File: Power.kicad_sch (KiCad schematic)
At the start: 11 parts, among them J14 Conn_01x02, U4 TPS62130

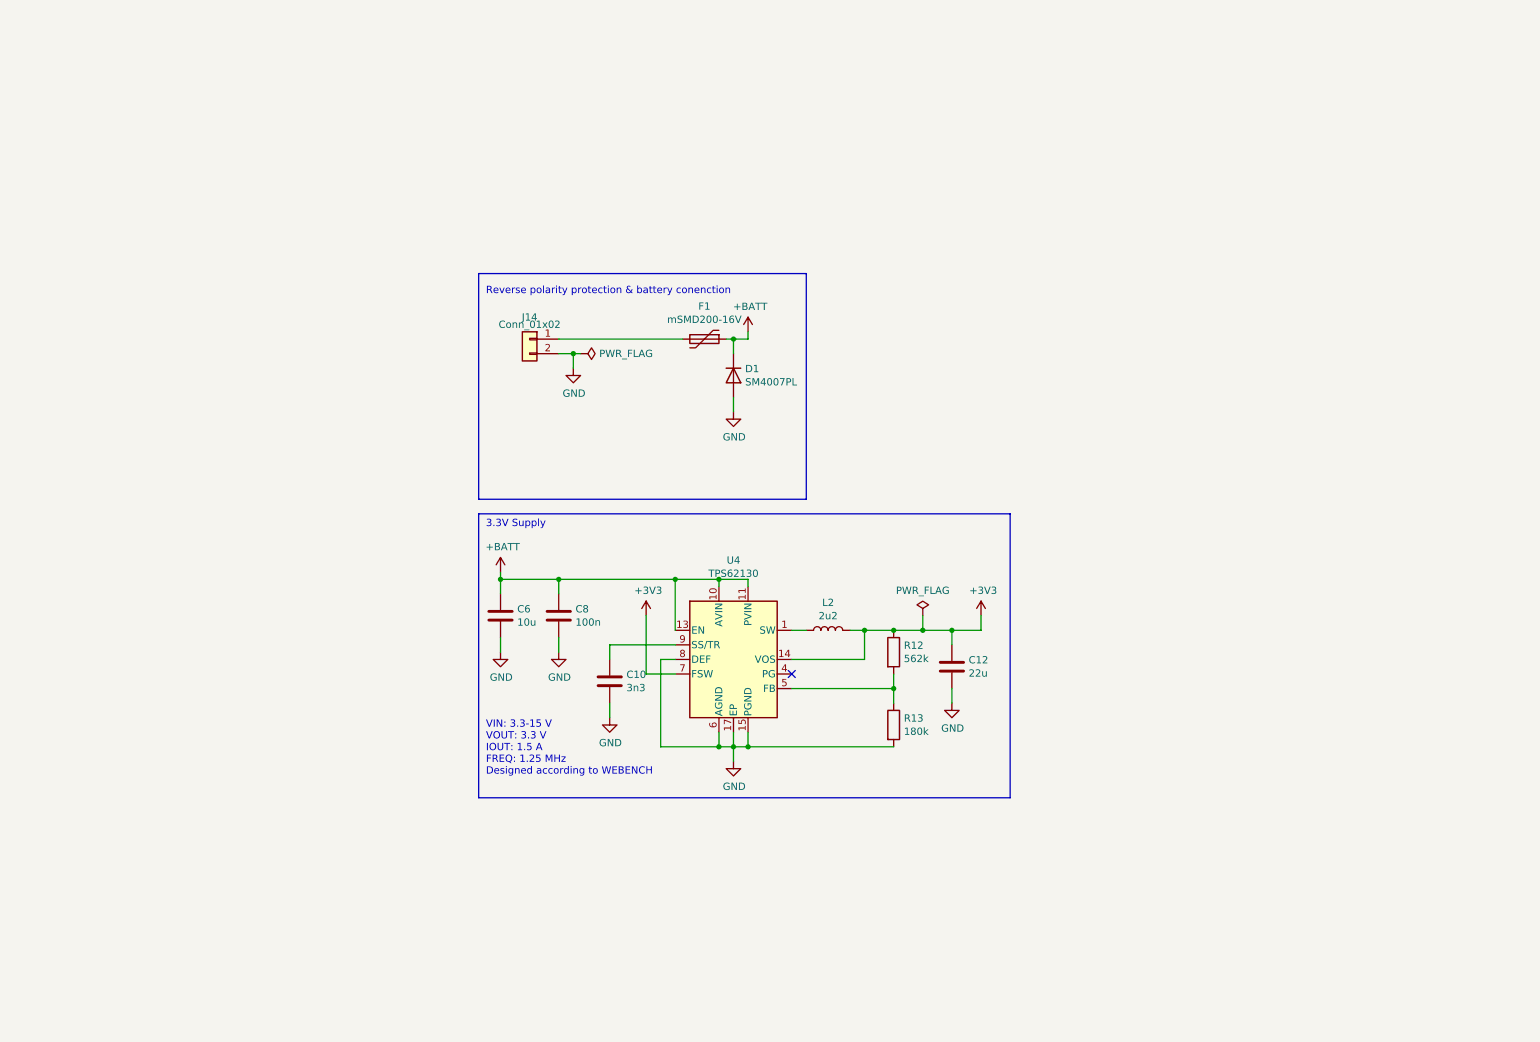
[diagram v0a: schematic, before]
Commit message: Move to KiCad v6, redesign circuit for chamber
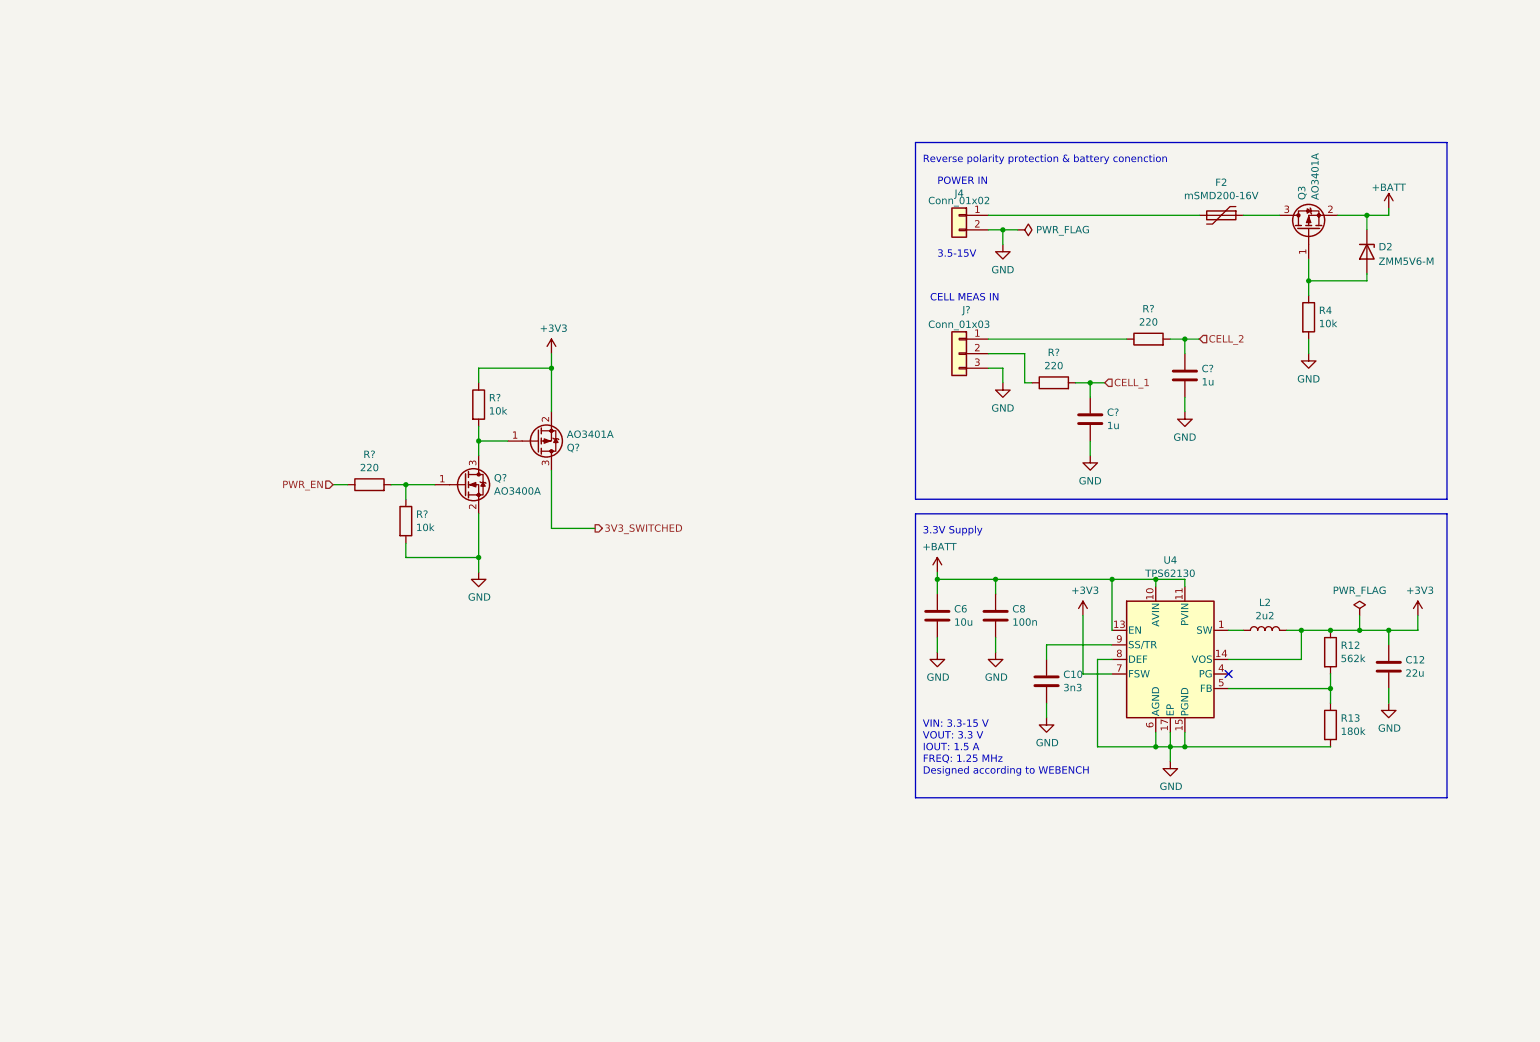
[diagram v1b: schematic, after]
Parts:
- removed D1: SM4007PL, Diode_SMD:D_SOD-123F, symbol Device:D
- removed F1: mSMD200-16V, Fuse:Fuse_1812_4532Metric, symbol Device:Polyfuse
- removed J14: Conn_01x02, Connector_JST:JST_XH_B2B-XH-AM_1x02_P2.50mm_Vertical, symbol Connector_Generic:Conn_01x02
- added C? (x2): 1u, Capacitor_SMD:C_0603_1608Metric, symbol Device:C
- added D2: ZMM5V6-M, Diode_SMD:D_MiniMELF, symbol Device:D_Zener
- added F2: mSMD200-16V, Fuse:Fuse_1812_4532Metric, symbol Device:Polyfuse
- added J4: Conn_01x02, Connector_JST:JST_XH_B2B-XH-AM_1x02_P2.50mm_Vertical, symbol Connector_Generic:Conn_01x02
- added J?: Conn_01x03, Connector_JST:JST_XH_B3B-XH-AM_1x03_P2.50mm_Vertical, symbol Connector_Generic:Conn_01x03
- added Q3, Q?: AO3401A, Package_TO_SOT_SMD:SOT-23, symbol Transistor_FET:AO3401A
- added Q?: AO3400A, Package_TO_SOT_SMD:SOT-23, symbol Transistor_FET:AO3400A
- added R4, R? (x2): 10k, Resistor_SMD:R_0603_1608Metric, symbol Device:R
- added R? (x3): 220, Resistor_SMD:R_0603_1608Metric, symbol Device:R
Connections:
- net +3V3: now also Q?.2 (S), R?.1
- net +BATT: now also D2.1 (K), Q3.2 (S)
- net GND: now also C?.2, C?.2, J4.2 (Pin_2), J?.3 (Pin_3), Q?.2 (S), R4.2, R?.2
- new net: D2.2 (A), Q3.1 (G), R4.1
- new net: F2.2, J4.1 (Pin_1)
- new net: F2.1, Q3.3 (D)
- new net: Q?.1 (G), R?.1, R?.2
- new net: Q?.1 (G), Q?.3 (D), R?.2
- new net: J?.1 (Pin_1), R?.1
- new net: J?.2 (Pin_2), R?.1
- new net 3V3_SWITCHED: Q?.3 (D)
- new net CELL_1: C?.1, R?.2
- new net CELL_2: C?.1, R?.2
- new net PWR_EN: R?.1
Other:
- note added: "3.5-15V"
- note added: "CELL MEAS IN"
- note added: "POWER IN"
- moved on the sheet: C10, C12, C6, C8, L2, R12, R13, U4

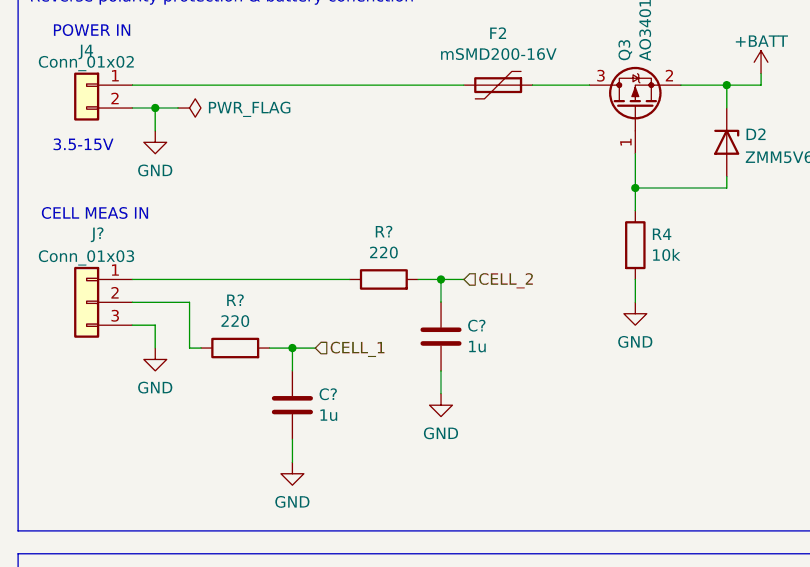
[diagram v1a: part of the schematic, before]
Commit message: Add test points, add JLC part numbers to JST XH connectors, clean up
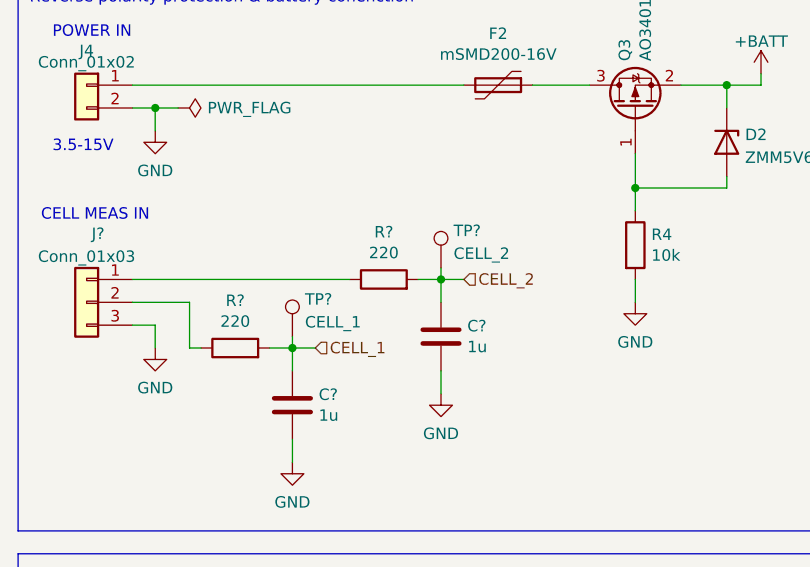
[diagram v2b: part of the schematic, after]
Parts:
- added TP?: CELL_1, symbol Connector:TestPoint
- added TP?: CELL_2, symbol Connector:TestPoint
- J4: LCSC (none) -> C20079
- J?: LCSC (none) -> C2316
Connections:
- net CELL_1: now also TP?.1
- net CELL_2: now also TP?.1
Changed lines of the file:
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@@
+    (stroke (width 0) (type default) (color 0 0 0 0))
+  )
+  (wire (pts (xy 220.98 71.12) (xy 220.98 72.39))
     (stroke (width 0) (type default) (color 0 0 0 0))
   )
@@
   )
   (wire (pts (xy 208.28 123.19) (xy 208.28 114.3))
+    (stroke (width 0) (type default) (color 0 0 0 0))
+  )
+  (wire (pts (xy 204.47 78.74) (xy 204.47 80.01))
     (stroke (width 0) (type default) (color 0 0 0 0))
   )
@@
       (effects (font (size 1.27 1.27)) hide)
     )
+    (property "LCSC" "C20079" (id 4) (at 181.61 50.8 0)
+      (effects (font (size 1.27 1.27)) hide)
+    )
     (pin "1")
     (pin "2")
@@
     (pin "2")
   )
+  (symbol (lib_id "Connector:TestPoint") (at 204.47 78.74 0) (unit 1)
+    (in_bom yes) (on_board yes) (fields_autoplaced)
+    (property "Reference" "TP?" (id 0) (at 205.867 74.6033 0)
+      (effects (font (size 1.27 1.27)) (justify left))
+    )
+    (property "Value" "CELL_1" (id 1) (at 205.867 77.1402 0)
+      (effects (font (size 1.27 1.27)) (justify left))
+    )
+    (property "Footprint" "" (id 2) (at 209.55 78.74 0)
+      (effects (font (size 1.27 1.27)) hide)
+    )
+    (property "Datasheet" "~" (id 3) (at 209.55 78.74 0)
+      (effects (font (size 1.27 1.27)) hide)
+    )
+    (pin "1")
+  )
   (symbol (lib_id "power:+3V3") (at 110.49 74.93 0) (unit 1)
     (in_bom yes) (on_board yes)
@@
       (effects (font (size 1.27 1.27)) hide)
     )
+    (property "LCSC" "C2316" (id 4) (at 181.61 74.93 0)
+      (effects (font (size 1.27 1.27)) hide)
+    )
     (pin "1")
     (pin "2")
@@
     (pin "3")
   )
+  (symbol (lib_id "Connector:TestPoint") (at 220.98 71.12 0) (unit 1)
+    (in_bom yes) (on_board yes) (fields_autoplaced)
+    (property "Reference" "TP?" (id 0) (at 222.377 66.9833 0)
+      (effects (font (size 1.27 1.27)) (justify left))
+    )
+    (property "Value" "CELL_2" (id 1) (at 222.377 69.5202 0)
+      (effects (font (size 1.27 1.27)) (justify left))
+    )
+    (property "Footprint" "" (id 2) (at 226.06 71.12 0)
+      (effects (font (size 1.27 1.27)) hide)
+    )
+    (property "Datasheet" "~" (id 3) (at 226.06 71.12 0)
+      (effects (font (size 1.27 1.27)) hide)
+    )
+    (pin "1")
+  )
   (symbol (lib_id "power:PWR_FLAG") (at 191.77 53.34 270) (unit 1)

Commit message: Add testpoint footprint assignments
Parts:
- TP16, TP17: renamed from TP?; footprint (none) -> TestPoint:TestPoint_Loop_D2.50mm_Drill1.0mm_LowProfile
- gave numbers to parts that had none: 10
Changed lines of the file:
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@@
   (symbol (lib_id "power:GND") (at 97.79 113.03 0) (unit 1)
     (in_bom yes) (on_board yes)
-    (property "Reference" "#PWR?" (id 0) (at 97.79 119.38 0)
+    (property "Reference" "#PWR0119" (id 0) (at 97.79 119.38 0)
       (effects (font (size 1.27 1.27)) hide)
     )
@@
   (symbol (lib_id "power:GND") (at 189.23 80.01 0) (unit 1)
     (in_bom yes) (on_board yes) (fields_autoplaced)
-    (property "Reference" "#PWR?" (id 0) (at 189.23 86.36 0)
+    (property "Reference" "#PWR0122" (id 0) (at 189.23 86.36 0)
       (effects (font (size 1.27 1.27)) hide)
     )
@@
   (symbol (lib_id "Device:R") (at 85.09 104.14 0) (unit 1)
     (in_bom yes) (on_board yes)
-    (property "Reference" "R?" (id 0) (at 86.868 102.9716 0)
+    (property "Reference" "R5" (id 0) (at 86.868 102.9716 0)
       (effects (font (size 1.27 1.27)) (justify left))
     )
@@
   (symbol (lib_id "Connector:TestPoint") (at 204.47 78.74 0) (unit 1)
     (in_bom yes) (on_board yes) (fields_autoplaced)
-    (property "Reference" "TP?" (id 0) (at 205.867 74.6033 0)
+    (property "Reference" "TP16" (id 0) (at 205.867 74.6033 0)
       (effects (font (size 1.27 1.27)) (justify left))
     )
@@
       (effects (font (size 1.27 1.27)) (justify left))
     )
-    (property "Footprint" "" (id 2) (at 209.55 78.74 0)
+    (property "Footprint" "TestPoint:TestPoint_Loop_D2.50mm_Drill1.0mm_LowProfile" (id 2) (at 209.55 78.74 0)
       (effects (font (size 1.27 1.27)) hide)
     )
@@
   (symbol (lib_id "power:+3V3") (at 110.49 74.93 0) (unit 1)
     (in_bom yes) (on_board yes)
-    (property "Reference" "#PWR?" (id 0) (at 110.49 78.74 0)
+    (property "Reference" "#PWR0118" (id 0) (at 110.49 78.74 0)
       (effects (font (size 1.27 1.27)) hide)
     )
@@
   (symbol (lib_id "Device:R") (at 97.79 83.82 0) (unit 1)
     (in_bom yes) (on_board yes)
-    (property "Reference" "R?" (id 0) (at 99.568 82.6516 0)
+    (property "Reference" "R6" (id 0) (at 99.568 82.6516 0)
       (effects (font (size 1.27 1.27)) (justify left))
     )
@@
   (symbol (lib_id "power:GND") (at 204.47 92.71 0) (unit 1)
     (in_bom yes) (on_board yes) (fields_autoplaced)
-    (property "Reference" "#PWR?" (id 0) (at 204.47 99.06 0)
+    (property "Reference" "#PWR0120" (id 0) (at 204.47 99.06 0)
       (effects (font (size 1.27 1.27)) hide)
     )
@@
   (symbol (lib_id "Device:R") (at 214.63 72.39 90) (unit 1)
     (in_bom yes) (on_board yes)
-    (property "Reference" "R?" (id 0) (at 214.63 67.1322 90))
+    (property "Reference" "R8" (id 0) (at 214.63 67.1322 90))
     (property "Value" "220" (id 1) (at 214.63 69.4436 90))
     (property "Footprint" "Resistor_SMD:R_0603_1608Metric" (id 2) (at 214.63 74.168 90)
@@
   (symbol (lib_id "power:GND") (at 220.98 85.09 0) (unit 1)
     (in_bom yes) (on_board yes) (fields_autoplaced)
-    (property "Reference" "#PWR?" (id 0) (at 220.98 91.44 0)
+    (property "Reference" "#PWR0121" (id 0) (at 220.98 91.44 0)
       (effects (font (size 1.27 1.27)) hide)
     )
@@
   (symbol (lib_id "Device:C") (at 204.47 86.36 0) (unit 1)
     (in_bom yes) (on_board yes)
-    (property "Reference" "C?" (id 0) (at 207.391 85.1916 0)
+    (property "Reference" "C1" (id 0) (at 207.391 85.1916 0)
       (effects (font (size 1.27 1.27)) (justify left))
     )
@@
   (symbol (lib_id "Device:R") (at 78.74 97.79 90) (unit 1)
     (in_bom yes) (on_board yes)
-    (property "Reference" "R?" (id 0) (at 78.74 92.5322 90))
+    (property "Reference" "R3" (id 0) (at 78.74 92.5322 90))
     (property "Value" "220" (id 1) (at 78.74 94.8436 90))
     (property "Footprint" "Resistor_SMD:R_0603_1608Metric" (id 2) (at 78.74 99.568 90)
@@
   (symbol (lib_id "Connector_Generic:Conn_01x03") (at 181.61 74.93 0) (mirror y) (unit 1)
     (in_bom yes) (on_board yes)
-    (property "Reference" "J?" (id 0) (at 182.88 67.31 0))
+    (property "Reference" "J9" (id 0) (at 182.88 67.31 0))
     (property "Value" "Conn_01x03" (id 1) (at 181.61 69.85 0))
     (property "Footprint" "Connector_JST:JST_XH_B3B-XH-AM_1x03_P2.50mm_Vertical" (id 2) (at 181.61 74.93 0)
@@
   (symbol (lib_id "Device:C") (at 220.98 78.74 0) (unit 1)
     (in_bom yes) (on_board yes)
-    (property "Reference" "C?" (id 0) (at 223.901 77.5716 0)
+    (property "Reference" "C2" (id 0) (at 223.901 77.5716 0)
       (effects (font (size 1.27 1.27)) (justify left))
     )
@@
   (symbol (lib_id "Transistor_FET:AO3400A") (at 95.25 97.79 0) (unit 1)
     (in_bom yes) (on_board yes)
-    (property "Reference" "Q?" (id 0) (at 100.457 96.6216 0)
+    (property "Reference" "Q1" (id 0) (at 100.457 96.6216 0)
       (effects (font (size 1.27 1.27)) (justify left))
     )
@@
   (symbol (lib_id "Device:R") (at 198.12 80.01 90) (unit 1)
     (in_bom yes) (on_board yes)
-    (property "Reference" "R?" (id 0) (at 198.12 74.7522 90))
+    (property "Reference" "R7" (id 0) (at 198.12 74.7522 90))
     (property "Value" "220" (id 1) (at 198.12 77.0636 90))
     (property "Footprint" "Resistor_SMD:R_0603_1608Metric" (id 2) (at 198.12 81.788 90)
@@
   (symbol (lib_id "Transistor_FET:AO3401A") (at 107.95 90.17 0) (mirror x) (unit 1)
     (in_bom yes) (on_board yes)
-    (property "Reference" "Q?" (id 0) (at 113.157 91.3384 0)
+    (property "Reference" "Q2" (id 0) (at 113.157 91.3384 0)
       (effects (font (size 1.27 1.27)) (justify left))
     )
@@
   (symbol (lib_id "Connector:TestPoint") (at 220.98 71.12 0) (unit 1)
     (in_bom yes) (on_board yes) (fields_autoplaced)
-    (property "Reference" "TP?" (id 0) (at 222.377 66.9833 0)
+    (property "Reference" "TP17" (id 0) (at 222.377 66.9833 0)
       (effects (font (size 1.27 1.27)) (justify left))
     )
@@
       (effects (font (size 1.27 1.27)) (justify left))
     )
-    (property "Footprint" "" (id 2) (at 226.06 71.12 0)
-      (effects (font (size 1.27 1.27)) hide)
-    )
+    (property "Footprint" "TestPoint:TestPoint_Loop_D2.50mm_Drill1.0mm_LowProfile" (id 2) (at 226.06 71.12 0)
+      (effects (font (size 1.27 1.27)) hide)
+    )

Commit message: Finalize schematic
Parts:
- R9: renamed from R4; value 10k -> 1M; LCSC C25804 -> C22935
- renumbered C6 to C1, C8 to C2, C10 to C3, C1 to C4, C2 to C5, C12 to C6, F2 to F1, J4 to J7, J9 to J8, L2 to L1, R12 to R10, R13 to R11, R3 to R4, TP16 to TP14, TP17 to TP15, U4 to U1
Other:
- note added: "Peak current on 3V3 switched rail: 3760 mA"
- note added: "Switched 3V3 rail"
- note added: "VIN: 3.3-15 V VOUT: 3.3 V IOUT: 3 A FREQ: 1.25 MHz Designed according to WEBENCH"
- note removed: "VIN: 3.3-15 V VOUT: 3.3 V IOUT: 1.5 A FREQ: 1.25 MHz Designed according to WEBENCH"
- title: (none) -> CO2 Chamber - Power
- moved on the sheet: C1, C2, C3, C4, C5, C6, D2, F1, J7, J8, L1, Q1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

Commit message: Start redesign for rev. 2
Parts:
- added R?: 10k, symbol Device:R
- added R? (x2): R, symbol Device:R
- added U?: BQ24074RGT, Package_DFN_QFN:VQFN-16-1EP_3x3mm_P0.5mm_EP1.6x1.6mm, symbol Battery_Management:BQ24074RGT
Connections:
- net GND: now also J7.1 (Pin_1), U?.17 (VSS), U?.8 (VSS); no longer J7.2 (Pin_2)
- net at F1.2: now also J7.2 (Pin_2); no longer J7.1 (Pin_1)
- new net: U?.10 (OUT), U?.11 (OUT)
- new net: U?.2 (BAT), U?.3 (BAT)
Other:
- moved on the sheet: C1, C2, C3, C6, J7, L1, Q1, Q2, R10, R11, R4, R5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

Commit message: Checkpoint
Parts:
- removed C4, C5: 1u, Capacitor_SMD:C_0603_1608Metric, symbol Device:C
- removed J8: Conn_01x03, Connector_JST:JST_XH_B3B-XH-AM_1x03_P2.50mm_Vertical, symbol Connector_Generic:Conn_01x03
- removed R7, R8: 220, Resistor_SMD:R_0603_1608Metric, symbol Device:R
- removed TP14: CELL_1, TestPoint:TestPoint_Loop_D2.50mm_Drill1.0mm_LowProfile, symbol Connector:TestPoint
- removed TP15: CELL_2, TestPoint:TestPoint_Loop_D2.50mm_Drill1.0mm_LowProfile, symbol Connector:TestPoint
- added C?: 10u, Capacitor_SMD:C_0805_2012Metric, symbol Device:C
- added C?: 220u, Capacitor_THT:CP_Radial_D8.0mm_P3.50mm, symbol Device:C_Polarized
- added J?: Conn_01x02, Connector_JST:JST_XH_B2B-XH-AM_1x02_P2.50mm_Vertical, symbol Connector_Generic:Conn_01x02
- added Q?: SS8550 Y2, symbol Device:Q_PNP_BEC
- added Q?: AO3400A, Package_TO_SOT_SMD:SOT-23, symbol Transistor_FET:AO3400A
- added Q?: AO3401A, Package_TO_SOT_SMD:SOT-23, symbol Transistor_FET:AO3401A
- added R?: 1k5, symbol Device:R
- added R? (x2): 15k, symbol Device:R
- added R? (x2): 3R3, symbol Device:R
- added R? (x3): 10k, symbol Device:R
- added R?: (no value), symbol Device:R
- added R?: 82k, symbol Device:R
- added U?: (no value), symbol Reference_Voltage:TL431PK
- R?: value R -> 5k6
- R?: value R -> 560
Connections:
- net +3V3: now also C?.1
- net +BATT: now also U?.2 (BAT), U?.3 (BAT); no longer C1.1, C2.1, U1.10 (AVIN), U1.11 (PVIN), U1.12 (PVIN), U1.13 (EN)
- net 3V3_SWITCHED: now also Q?.2 (S), R?.1, R?.1
- net GND: now also R?.1, R?.1, R?.2, U?.14 (TMR), U?.6 (EN1), C?.2, C?.2, J?.1 (Pin_1), Q?.2 (S), R?.1, R?.1, R?.2, R?.2, R?.2, R?.2, U?.2 (A)
- net at R?.1: now also U?.1 (TS)
- net at R?.2: now also U?.15 (ITERM)
- net PWR_OUT: now reaches U?.10 (OUT), U?.11 (OUT)
- net PWR_OUT: now also C1.1, C2.1, U1.10 (AVIN), U1.11 (PVIN), U1.12 (PVIN), U1.13 (EN), U?.5 (EN2), C?.1
- net at U?.12 (ILIM): now also R?.2
- net at U?.13 (IN): now also J?.2 (Pin_2)
- net at U?.16 (ISET): now also R?.2
- net at U?.4 (~{CE}): now also R?.2
- new net: R?.1, R?.2, U?.1 (REF)
- new net: Q?.3 (D), R?.2
- new net: Q?.1 (G), Q?.2 (E), R?.1
- new net: Q?.1 (B), R?.1, R?.2
- new net: Q?.3 (D), R?.1
- new net: Q?.1 (G), R?.2, U?.3 (K)
- no-connect marks 1 -> 3
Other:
- note added: "3.3-4.2 V (1S9P)"
- note added: "4.4V-10V"
- note added: "BATTERY IN"
- note added: "ISET set to 890/1500 = 593 mA ITERM set to 5600 * 0.03 / 1500 = 112 mA ILIM set to 1550 / 560 = 2.77 A"
- note added: "SOLAR IN"
- note added: "Solar charging, undervoltage lockout and power path management"
- note added: "Switched 3V3 rail and overvoltage clamping"
- note removed: "3.5-15V"
- note removed: "CELL MEAS IN"
- note removed: "POWER IN"
- note removed: "Switched 3V3 rail"
- moved on the sheet: C1, C2, C3, C6, D2, F1, J7, L1, Q1, Q2, Q3, R10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
